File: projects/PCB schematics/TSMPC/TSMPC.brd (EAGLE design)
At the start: 62.2 x 47.9 mm, 16 parts, among them X1 AS06-05

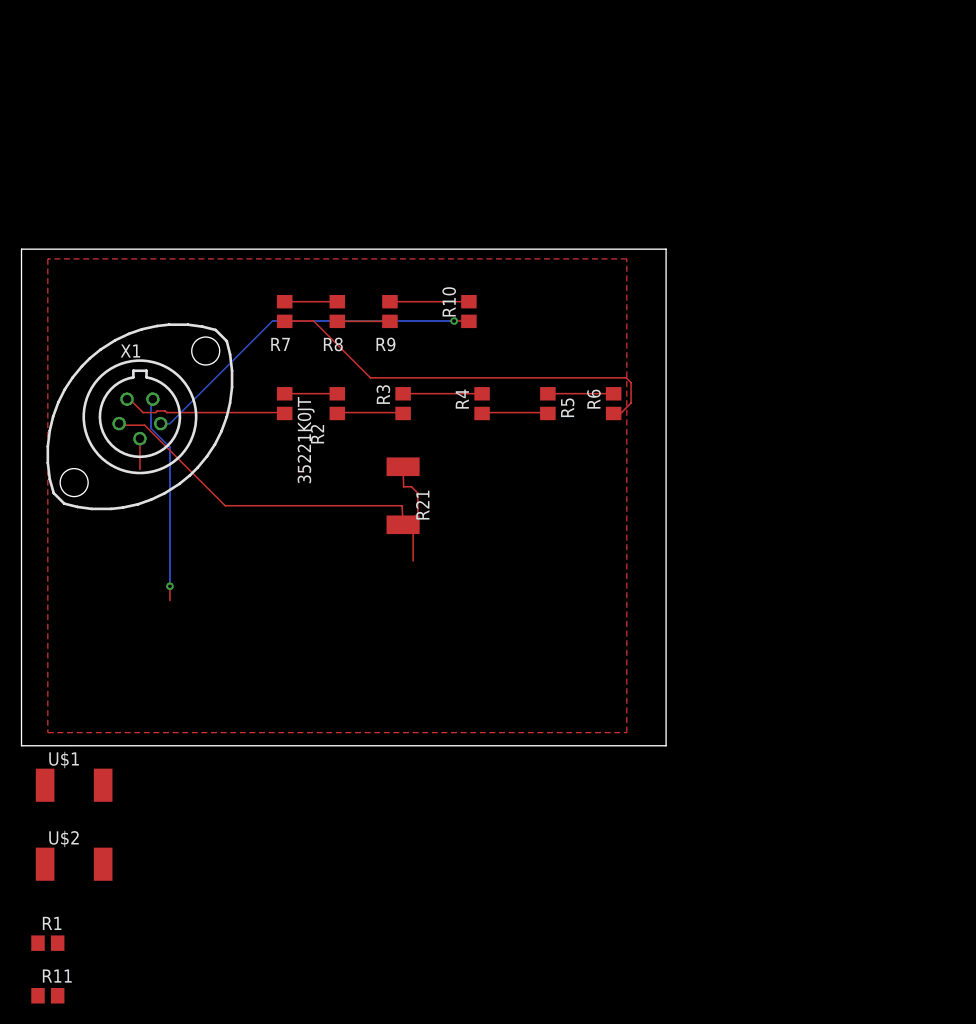
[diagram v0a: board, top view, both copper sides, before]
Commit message: TSMPC - Initial revision.
Completed board, minus the connector. Still needs verification from @michaelpass .
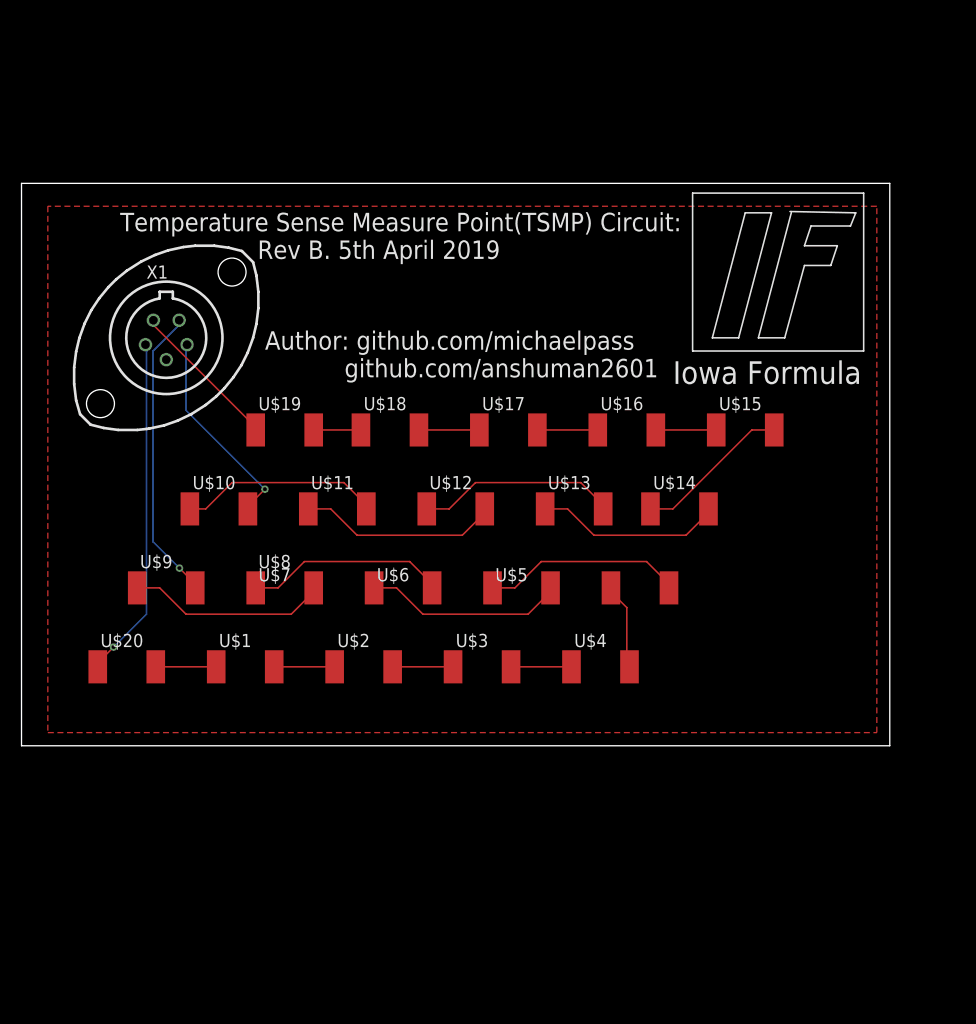
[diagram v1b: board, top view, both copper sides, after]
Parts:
- removed 35221K0JT, R10, R2, R3, R4, R5, R6, R7, R8, R9: 1k, rcl:R0805
- removed R1, R11: (no value), rcl:R0805
- removed R21: 1k, rcl:R2512
- added U$10, U$11, U$12, U$13, U$14, U$15, U$16, U$17, U$18, U$19, U$20, U$3, U$4, U$5, U$6, U$7, U$8, U$9: 35221K0JT2512, IowaFormula:R2512
- moved U$2 33.8 mm to (33.0, 7.62)
- moved U$1 20.1 mm to (21.6, 7.62)
- moved X1 8.03 mm to (14.0, 39.4)
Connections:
- new net N$22: U$1.2, U$2.1
- new net N$23: U$2.2, U$3.1
- new net N$24: U$3.2, U$4.1
- new net N$25: U$4.2, U$5.1
- new net N$26: U$5.2, U$6.1
- new net N$27: U$6.2, U$7.1
- new net N$28: U$7.2, U$8.1
- new net N$29: U$8.2, U$9.1
- net HV+: now also U$19.1; no longer 35221K0JT.2
- net HV+_MEASURE_POINT: now also U$10.2; no longer R10.1
- net HV-: now also U$20.1; no longer R21.2
- net HV-_MEASURE_POINT: now also U$9.2
- net N$1: now also U$18.1, U$19.2; no longer 35221K0JT.1, R2.2
- net N$2: now also U$17.1, U$18.2; no longer R2.1, R3.2
- net N$21: now also U$1.1, U$20.2; no longer R21.1
- net N$3: now also U$16.1, U$17.2; no longer R3.1, R4.2
- net N$4: now also U$15.1, U$16.2; no longer R4.1, R5.2
- net N$5: now also U$14.1, U$15.2; no longer R5.1, R6.2
- net N$6: now also U$13.1, U$14.2; no longer R6.1, R7.2
- net N$7: now also U$12.1, U$13.2; no longer R7.1, R8.2
- net N$8: now also U$11.1, U$12.2; no longer R8.1, R9.2
- net N$9: now also U$10.1, U$11.2; no longer R10.2, R9.1
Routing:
- net N$6: track 40.0 -> 18.6 mm
- net N$28: track 0.00 -> 19.9 mm
- net N$27: track 0.00 -> 19.9 mm
- net N$26: track 0.00 -> 19.9 mm
- net N$29: track 0.00 -> 19.9 mm
- net N$8: track 5.08 -> 19.9 mm
- net N$7: track 5.08 -> 19.9 mm
- net HV+_MEASURE_POINT: track 33.9 -> 20.1 mm
- net N$9: track 7.62 -> 19.9 mm
- net N$25: track 0.00 -> 9.04 mm
- net HV-_MEASURE_POINT: track 20.3 -> 29.1 mm
- net N$5: track 6.37 -> 15.1 mm
- net N$24: track 0.00 -> 5.83 mm
- net N$23: track 0.00 -> 5.83 mm
- net N$22: track 0.00 -> 5.83 mm
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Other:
- board size 62.2 x 47.9 mm -> 83.8 x 54.3 mm
- board text added: "Author: github.com/michaelpass github.com/anshuman2601"
- board text added: "Iowa Formula"
- board text added: "Temperature Sense Measure Point(TSMP) Circuit: Rev B. 5th April 2019"

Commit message: TSMPC - Initial revisions from pull request #3.
Many changes were needed from Anshuman's initial pull request version. Half of the necessary changes have been made here. Connectors must be added. I believe we should also add in a seperate GND board and not have our chassis point on this board, so as to avoid potential isolation issues.
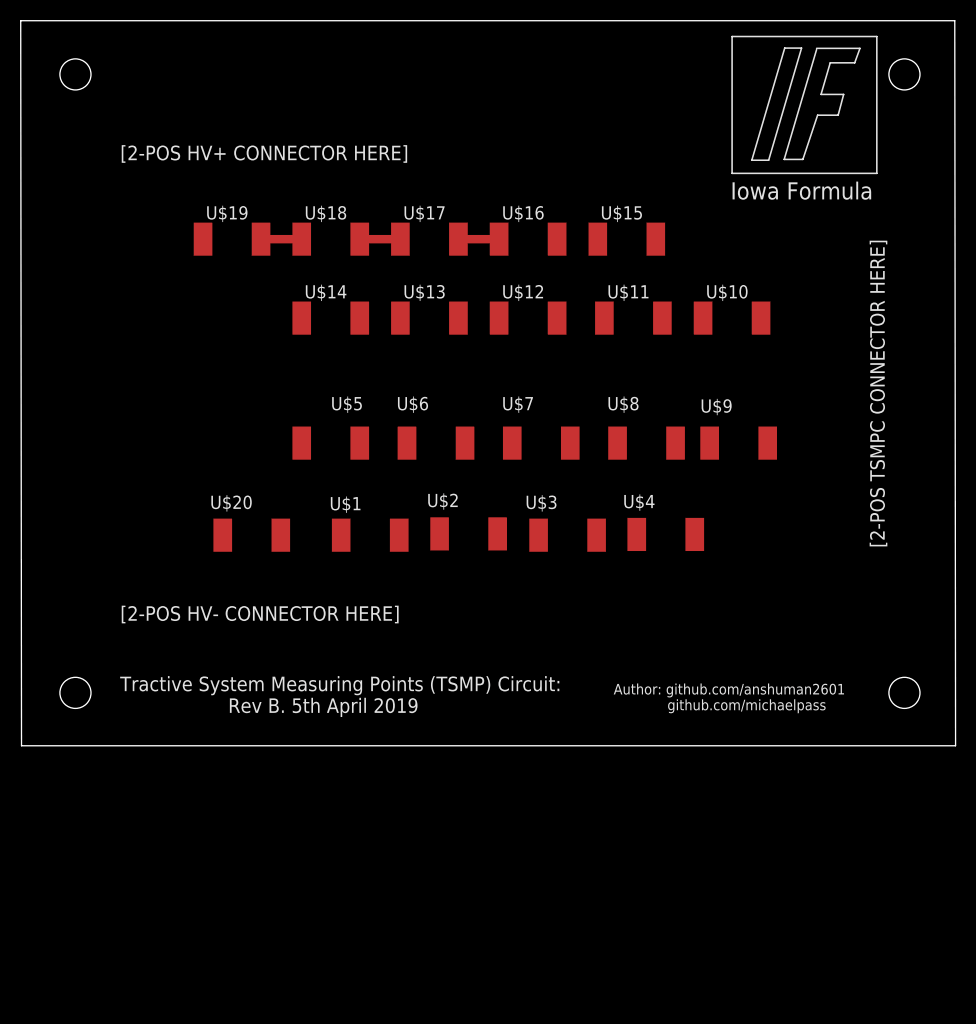
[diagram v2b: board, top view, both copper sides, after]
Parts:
- removed X1: AS06-05, con-deutsch:AS06-05
- moved U$9 57.0 mm to (69.2, 29.2)
- moved U$10 52.8 mm to (68.6, 41.3)
- moved U$14 38.4 mm to (29.8, 41.3)
- moved U$8 37.6 mm to (60.3, 29.2), turned to 180 degrees
- moved U$11 34.0 mm to (59.1, 41.3)
- moved U$5 33.0 mm to (29.8, 29.2)
- moved U$13 23.1 mm to (39.4, 41.3)
- moved U$15 21.7 mm to (58.4, 48.9)
- moved U$16 20.7 mm to (48.9, 48.9)
- moved U$17 19.9 mm to (39.4, 48.9)
- moved U$12 19.7 mm to (48.9, 41.3)
- moved U$7 19.3 mm to (50.2, 29.2)
- moved U$18 19.3 mm to (29.8, 48.9)
- moved U$19 19.1 mm to (20.3, 48.9)
- moved U$1 17.5 mm to (33.7, 20.3)
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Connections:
- removed net CHASSIS_GND: X1.3
- net HV+: no longer X1.1
- net HV+_MEASURE_POINT: no longer X1.4
- net HV-: no longer X1.2
- net HV-_MEASURE_POINT: no longer X1.5
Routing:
- net HV-: track 33.6 -> 0.38 mm, vias 1 -> 0
- net HV-_MEASURE_POINT: track 29.1 -> 0.00 mm, vias 1 -> 0
- net HV+_MEASURE_POINT: track 20.1 -> 0.00 mm, vias 1 -> 0
- net N$28: track 19.9 -> 0.00 mm
- net N$9: track 19.9 -> 0.00 mm
- net N$8: track 19.9 -> 0.00 mm
- net N$7: track 19.9 -> 0.00 mm
- net N$29: track 19.9 -> 0.00 mm
- net N$27: track 19.9 -> 0.38 mm
- net N$26: track 19.9 -> 0.38 mm
- net N$6: track 18.6 -> 0.00 mm
- net N$5: track 15.1 -> 0.00 mm
- net HV+: track 15.1 -> 0.26 mm
- net N$25: track 9.04 -> 0.26 mm
- net N$4: track 5.83 -> 0.00 mm
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- removed copper zone on layer 1, net GND
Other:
- board size 83.8 x 54.3 mm -> 90.2 x 70 mm
- board text added: "Author: github.com/anshuman2601 github.com/michaelpass"
- board text added: "Tractive System Measuring Points (TSMP) Circuit: Rev B. 5th April 2019"
- board text added: "[2-POS HV+ CONNECTOR HERE]"
- board text added: "[2-POS HV- CONNECTOR HERE]"
- board text added: "[2-POS TSMPC CONNECTOR HERE]"
- board text removed: "Author: github.com/michaelpass github.com/anshuman2601"
- board text removed: "Temperature Sense Measure Point(TSMP) Circuit: Rev B. 5th April 2019"

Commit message: TSMPC - Additional revisions for pull request #3.
Final revisions (apart from connectors and creation of simple GND board) have been done and are ready for review by Anshuman Sahu (and selection of HV connectors)

Squash - TSMPC - Fixed missing connection as per @rgoedken, PR#3.

Squash - TSMPC - Added connectors. PR#3 suggestions. Pending approval.
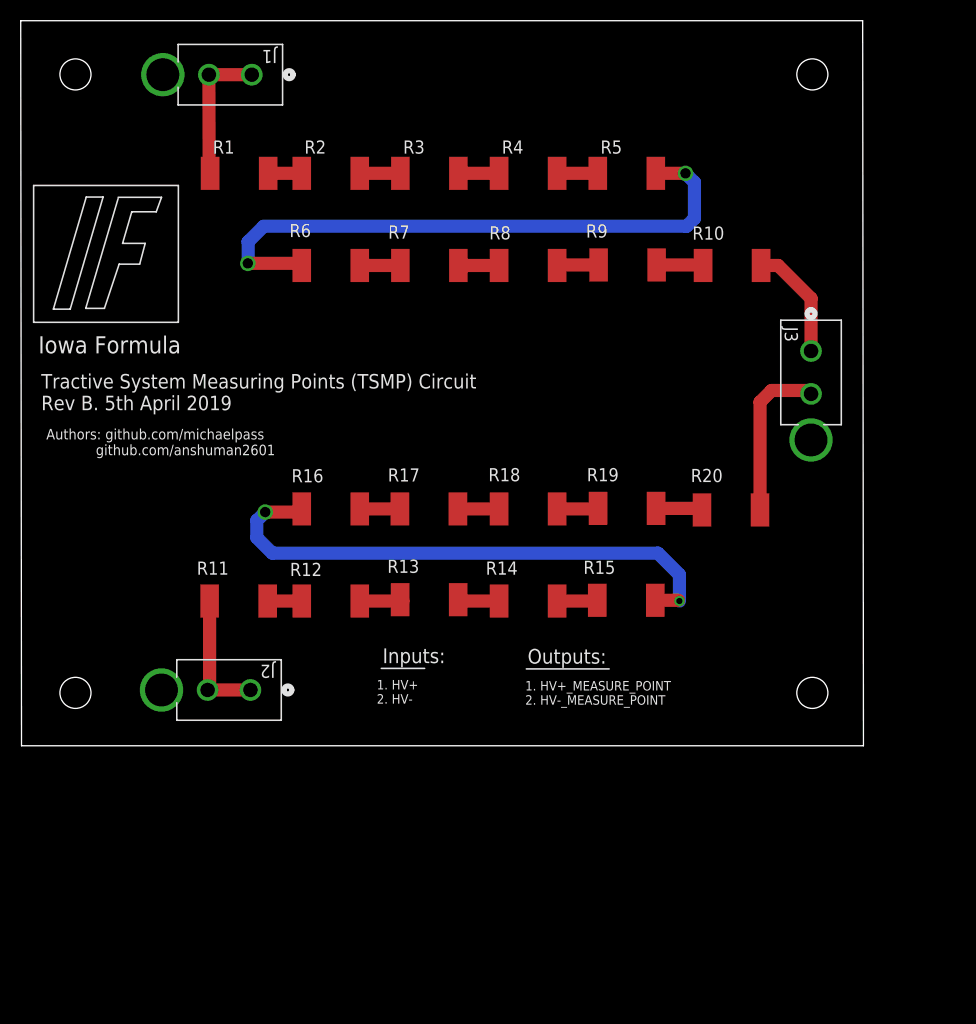
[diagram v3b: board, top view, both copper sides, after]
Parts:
- removed U$1, U$10, U$11, U$12, U$13, U$14, U$15, U$16, U$17, U$18, U$19, U$2, U$20, U$3, U$4, U$5, U$6, U$7, U$8, U$9: 35221K0JT2512, IowaFormula:R2512
- added J1, J2, J3: 2P_1-770166-0, con-MATE-N-LOK:CON2_1X2_P163_VMNL-1MTG
- added R1, R10, R11, R12, R13, R14, R15, R16, R17, R18, R19, R2, R20, R3, R4, R5, R6, R7, R8, R9: 35221K0JT2512, IowaFormula:R2512
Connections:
- net HV+: now also J1.1, J1.2, R1.1; no longer U$19.1
- net HV+_MEASURE_POINT: now also J3.1, R10.2; no longer U$10.2
- net HV-: now also J2.1, J2.2, R11.1; no longer U$20.1
- net HV-_MEASURE_POINT: now also J3.2, R20.2; no longer U$9.2
- net N$1: now also R1.2, R2.1; no longer U$18.1, U$19.2
- net N$2: now also R2.2, R3.1; no longer U$17.1, U$18.2
- net N$21: now also R11.2, R12.1; no longer U$1.1, U$20.2
- net N$22: now also R12.2, R13.1; no longer U$1.2, U$2.1
- net N$23: now also R13.2, R14.1; no longer U$2.2, U$3.1
- net N$24: now also R14.2, R15.1; no longer U$3.2, U$4.1
- net N$25: now also R15.2, R16.1; no longer U$4.2, U$5.1
- net N$26: now also R16.2, R17.1; no longer U$5.2, U$6.1
- net N$27: now also R17.2, R18.1; no longer U$6.2, U$7.1
- net N$28: now also R18.2, R19.1; no longer U$7.2, U$8.1
- net N$29: now also R19.2, R20.1; no longer U$8.2, U$9.1
- net N$3: now also R3.2, R4.1; no longer U$16.1, U$17.2
- net N$4: now also R4.2, R5.1; no longer U$15.1, U$16.2
- net N$5: now also R5.2, R6.1; no longer U$14.1, U$15.2
- net N$6: now also R6.2, R7.1; no longer U$13.1, U$14.2
- net N$7: now also R7.2, R8.1; no longer U$12.1, U$13.2
- net N$8: now also R8.2, R9.1; no longer U$11.1, U$12.2
- net N$9: now also R10.1, R9.2; no longer U$10.1, U$11.2
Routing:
- net N$5: track 0.00 -> 59.0 mm, vias 0 -> 2
- net N$25: track 0.26 -> 53.9 mm, vias 0 -> 2
- net HV-_MEASURE_POINT: track 0.00 -> 15.9 mm
- net HV+: track 0.26 -> 14.0 mm
- net HV-: track 0.38 -> 14.0 mm
- net HV+_MEASURE_POINT: track 0.00 -> 11.2 mm
- net N$9: track 0.00 -> 4.50 mm
- net N$29: track 0.00 -> 4.50 mm
- net N$22: track 0.00 -> 4.18 mm
- net N$8: track 0.00 -> 4.02 mm
- net N$23: track 0.00 -> 4.00 mm
- net N$27: track 0.38 -> 4.35 mm
- net N$28: track 0.00 -> 3.97 mm
- net N$7: track 0.00 -> 3.92 mm
- net N$6: track 0.00 -> 3.92 mm
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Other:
- board size 90.2 x 70 mm -> 81.3 x 70 mm
- board text added: "1. HV+ 2. HV-"
- board text added: "1. HV+_MEASURE_POINT 2. HV-_MEASURE_POINT"
- board text added: "Authors: github.com/michaelpass github.com/anshuman2601"
- board text added: "Inputs:"
- board text added: "Outputs:"
- board text added: "Tractive System Measuring Points (TSMP) Circuit Rev B. 5th April 2019"
- board text removed: "Author: github.com/anshuman2601 github.com/michaelpass"
- board text removed: "Tractive System Measuring Points (TSMP) Circuit: Rev B. 5th April 2019"
- board text removed: "[2-POS HV+ CONNECTOR HERE]"
- board text removed: "[2-POS HV- CONNECTOR HERE]"
- board text removed: "[2-POS TSMPC CONNECTOR HERE]"
